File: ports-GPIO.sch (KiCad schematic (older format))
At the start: 3 parts

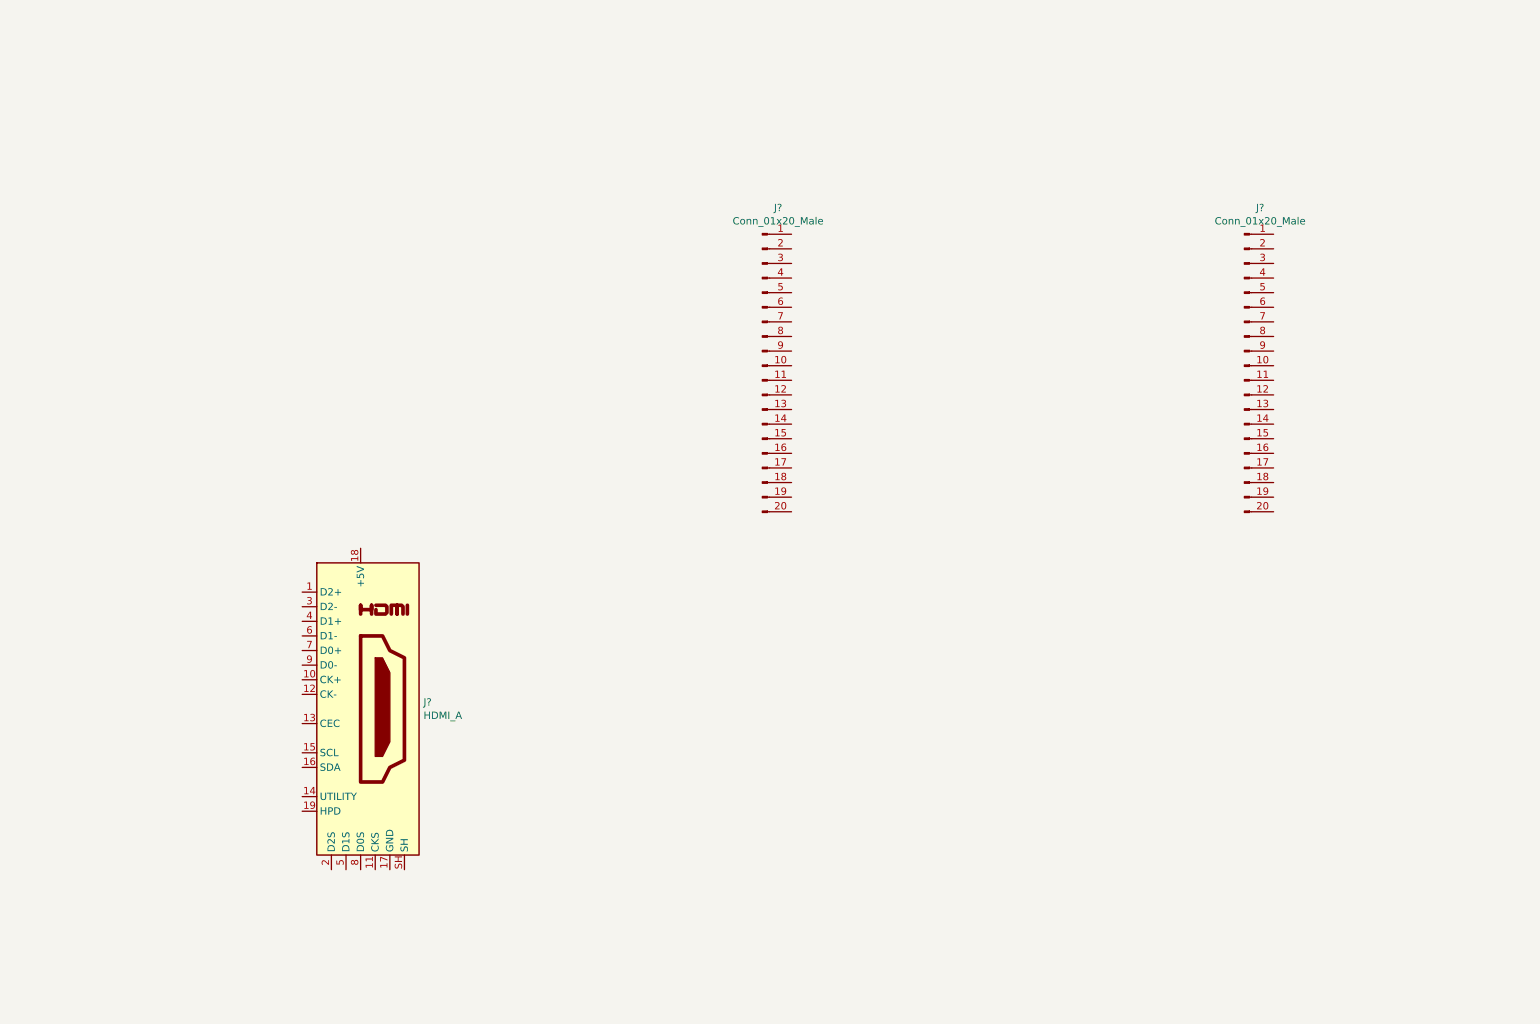
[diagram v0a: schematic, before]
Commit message: broke, out all GPIO and finsihed wiring HDMI
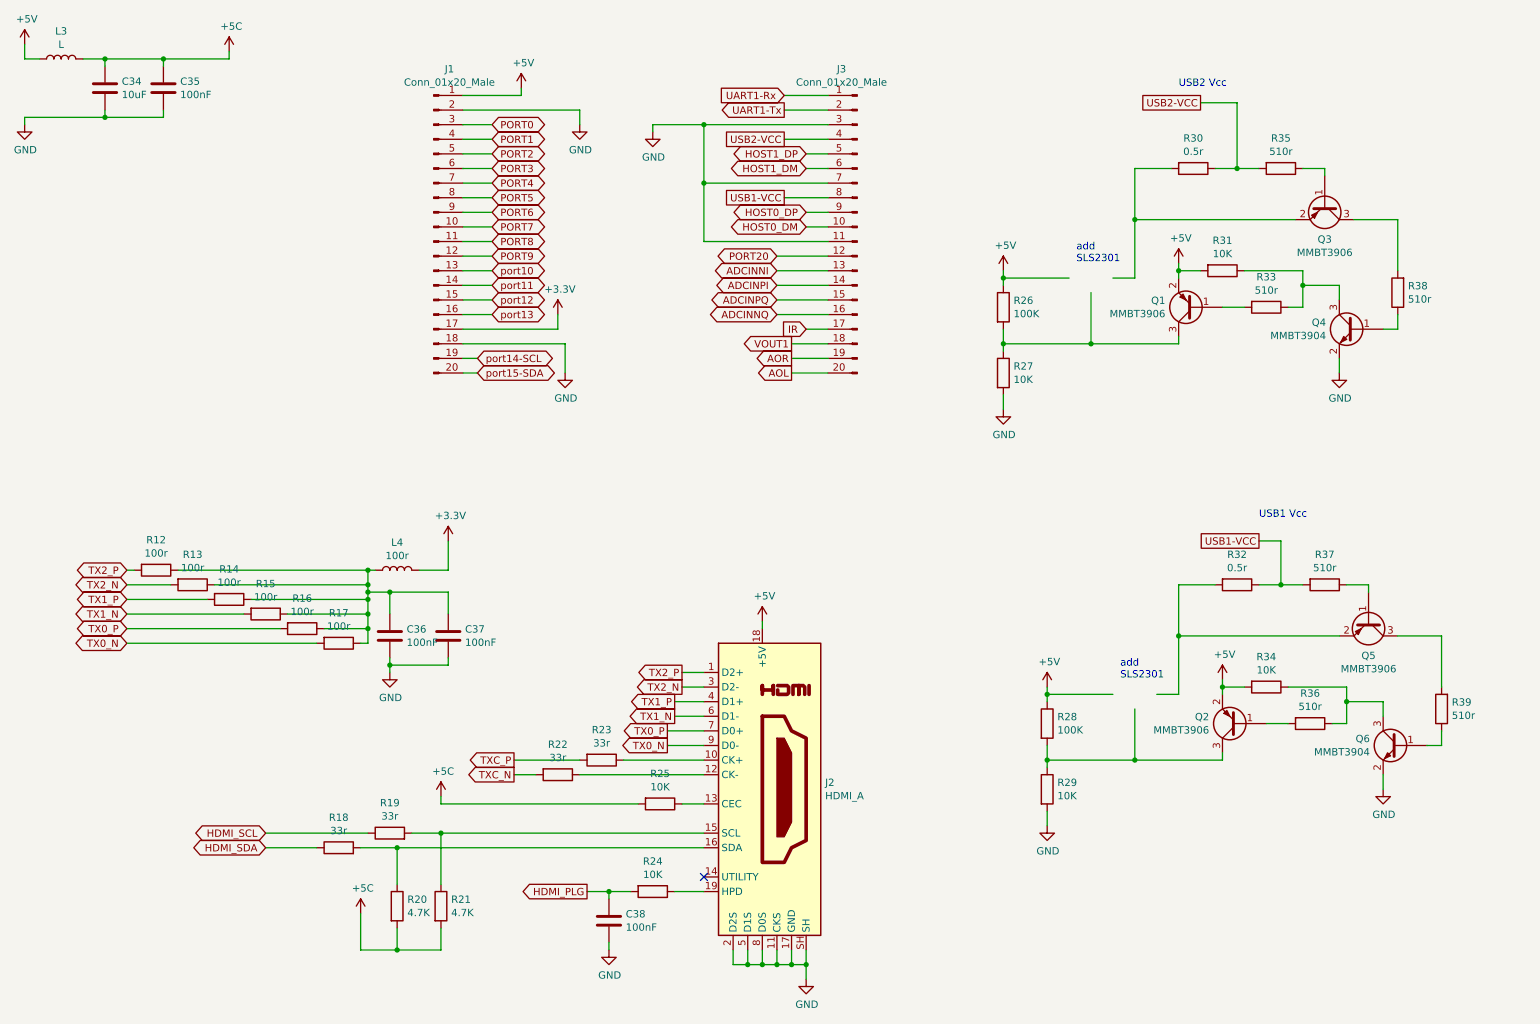
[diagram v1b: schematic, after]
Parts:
- added C34: 10uF, symbol Device:C
- added C35, C36, C37, C38: 100nF, symbol Device:C
- added L3: L, symbol Device:L
- added L4: 100r, symbol Device:L
- added Q1, Q2, Q3, Q5: MMBT3906, Package_TO_SOT_SMD:SOT-23, symbol Transistor_BJT:MMBT3906
- added Q4, Q6: MMBT3904, Package_TO_SOT_SMD:SOT-23, symbol Transistor_BJT:MMBT3904
- added R12, R13, R14, R15, R16, R17: 100r, symbol Device:R
- added R18, R19, R22, R23: 33r, symbol Device:R
- added R20, R21: 4.7K, symbol Device:R
- added R24, R25, R27, R29, R31, R34: 10K, symbol Device:R
- added R26, R28: 100K, symbol Device:R
- added R30, R32: 0.5r, symbol Device:R
- added R33, R35, R36, R37, R38, R39: 510r, symbol Device:R
- gave numbers to parts that had none: 3
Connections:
- net TX2_P: now reaches J2.1 (D2+)
- net TX2_P: now also R12.2
- net at J2.10 (CK+): now also R23.1
- net GND: now reaches J2.11 (CKS)
- net GND: now also J1.18 (Pin_18), J1.2 (Pin_2), J2.17 (GND), J2.2 (D2S), J2.5 (D1S), J2.8 (D0S), J2.SH, J3.11 (Pin_11), J3.3 (Pin_3), J3.7 (Pin_7), C34.2, C35.2, C36.2, C37.2, C38.2, Q4.2 (E), Q6.2 (E), R27.2, R29.2
- net at J2.12 (CK-): now also R22.1
- net at J2.13 (CEC): now also R25.1
- net at J2.15 (SCL): now also R19.2, R21.1
- net at J2.16 (SDA): now also R18.2, R20.1
- net +5V: now reaches J2.18 (+5V)
- net +5V: now also J1.1 (Pin_1), L3.1, Q1.2 (E), Q2.2 (E), R26.1, R28.1, R31.2, R34.2
- net at J2.19 (HPD): now also R24.1
- net TX2_N: now reaches J2.3 (D2-)
- net TX2_N: now also R13.2
- net TX1_P: now reaches J2.4 (D1+)
- net TX1_P: now also R14.2
- net TX1_N: now reaches J2.6 (D1-)
- net TX1_N: now also R15.2
- net TX0_P: now reaches J2.7 (D0+)
- net TX0_P: now also R16.2
- net TX0_N: now reaches J2.9 (D0-)
- net TX0_N: now also R17.2
- net UART1-Rx: now reaches J3.1 (Pin_1)
- net HOST0_DM: now reaches J3.10 (Pin_10)
- net PORT20: now reaches J3.12 (Pin_12)
- net ADCINNI: now reaches J3.13 (Pin_13)
- net ADCINPI: now reaches J3.14 (Pin_14)
- net ADCINPQ: now reaches J3.15 (Pin_15)
- net ADCINNQ: now reaches J3.16 (Pin_16)
- net IR: now reaches J3.17 (Pin_17)
- net VOUT1: now reaches J3.18 (Pin_18)
- net AOR: now reaches J3.19 (Pin_19)
- net UART1-Tx: now reaches J3.2 (Pin_2)
- net AOL: now reaches J3.20 (Pin_20)
- net USB2-VCC: now reaches J3.4 (Pin_4)
- net USB2-VCC: now also R30.1, R35.2
- net HOST1_DP: now reaches J3.5 (Pin_5)
- net HOST1_DM: now reaches J3.6 (Pin_6)
- net USB1-VCC: now reaches J3.8 (Pin_8)
- net USB1-VCC: now also R32.1, R37.2
- net HOST0_DP: now reaches J3.9 (Pin_9)
- net PORT7: now reaches J1.10 (Pin_10)
- net PORT8: now reaches J1.11 (Pin_11)
- net PORT9: now reaches J1.12 (Pin_12)
- net port10: now reaches J1.13 (Pin_13)
- net port11: now reaches J1.14 (Pin_14)
- net port12: now reaches J1.15 (Pin_15)
- net port13: now reaches J1.16 (Pin_16)
- net +3V3: now reaches J1.17 (Pin_17)
- net +3V3: now also L4.2
- net port14-SCL: now reaches J1.19 (Pin_19)
- net port15-SDA: now reaches J1.20 (Pin_20)
- net PORT0: now reaches J1.3 (Pin_3)
- net PORT1: now reaches J1.4 (Pin_4)
- net PORT2: now reaches J1.5 (Pin_5)
- net PORT3: now reaches J1.6 (Pin_6)
- net PORT4: now reaches J1.7 (Pin_7)
- net PORT5: now reaches J1.8 (Pin_8)
- net PORT6: now reaches J1.9 (Pin_9)
- new net: C36.1, C37.1, L4.1, R12.1, R13.1, R14.1, R15.1, R16.1, R17.1
- new net: Q2.3 (C), R28.2, R29.1
- new net: Q2.1 (B), R36.2
- new net: Q6.3 (C), R34.1, R36.1
- new net: Q6.1 (B), R39.1
- new net: Q5.3 (C), R39.2
- new net: Q5.1 (B), R37.1
- new net: Q5.2 (E), R32.2
- new net: Q1.3 (C), R26.2, R27.1
- new net: Q1.1 (B), R33.2
- new net: Q4.3 (C), R31.1, R33.1
- new net: Q4.1 (B), R38.1
- new net: Q3.3 (C), R38.2
- new net: Q3.1 (B), R35.1
- new net: Q3.2 (E), R30.2
- new net +5C: C34.1, C35.1, L3.2, R20.2, R21.2, R25.2
- new net HDMI_PLG: C38.1, R24.2
- new net HDMI_SCL: R19.1
- new net HDMI_SDA: R18.1
- new net TXC_N: R22.2
- new net TXC_P: R23.2
- no-connect marks 0 -> 1
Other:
- note added: "USB1 Vcc"
- note added: "USB2 Vcc"
- note added: "add\nSLS2301"
- moved on the sheet: J1, J2, J3

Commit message: added todo list before i feel aleeped on my keybard*
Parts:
- removed Q2, Q5: MMBT3906, Package_TO_SOT_SMD:SOT-23, symbol Transistor_BJT:MMBT3906
- removed Q6: MMBT3904, Package_TO_SOT_SMD:SOT-23, symbol Transistor_BJT:MMBT3904
- removed R28: 100K, symbol Device:R
- removed R29, R34: 10K, symbol Device:R
- removed R32: 0.5r, symbol Device:R
- removed R36, R37, R39: 510r, symbol Device:R
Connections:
- net labels removed: USB1-VCC
- wire segments 206 -> 173
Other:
- note added: "Reserved for Blue bean WIFI module"
- note removed: "USB1 Vcc"

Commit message: finished scimatic for now, and started populating PCB. *chugs rrum*
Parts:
- added U8: SLS2301, Package_TO_SOT_SMD:SOT-23, symbol Csky:SLS2301
- C34, C35, C36, C37, C38: footprint (none) -> Capacitor_SMD:C_0402_1005Metric
- J1, J3: footprint (none) -> Connector_PinSocket_2.54mm:PinSocket_1x20_P2.54mm_Vertical
- J2: footprint (none) -> Connector_HDMI:HDMI_Micro-D_Molex_46765-0x01
- L3, L4: footprint (none) -> Inductor_SMD:L_0402_1005Metric
- R12, R13, R14, R16, R17: value 100r -> 100R; footprint (none) -> Resistor_SMD:R_0402_1005Metric
- R15: footprint (none) -> Resistor_SMD:R_0402_1005Metric
- R18, R19, R22, R23: value 33r -> 33R; footprint (none) -> Resistor_SMD:R_0402_1005Metric
- R20, R21: value 4.7K -> 4.7k; footprint (none) -> Resistor_SMD:R_0402_1005Metric
- R24, R25, R27, R31: value 10K -> 10k; footprint (none) -> Resistor_SMD:R_0402_1005Metric
- R26: value 100K -> 100k; footprint (none) -> Resistor_SMD:R_0402_1005Metric
- R30: value 0.5r -> 0.5R; footprint (none) -> Resistor_SMD:R_0402_1005Metric
- R33, R35, R38: value 510r -> 510R; footprint (none) -> Resistor_SMD:R_0402_1005Metric
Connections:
- net labels removed: HOST0_DM, HOST0_DP
- wire segments 173 -> 171
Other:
- note removed: "Reserved for Blue bean WIFI module"
- note removed: "add\nSLS2301"
- moved on the sheet: R26, R27

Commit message: started layout of the PCB, allso moved onto craken rum, from captin morgan. please for the love of god check the footprints are right. @MAX
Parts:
- added J4: USB_B_Micro, Connector_USB:USB_Micro-B_Amphenol_10103594-0001LF_Horizontal, symbol Connector:USB_B_Micro
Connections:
- net +5V: now also J4.1 (VBUS)
- net GND: now also J4.5 (GND), J4.6 (Shield)
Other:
- moved on the sheet: Q1, Q3, Q4, R26, R27, R30, R31, R33, R35, R38, U8

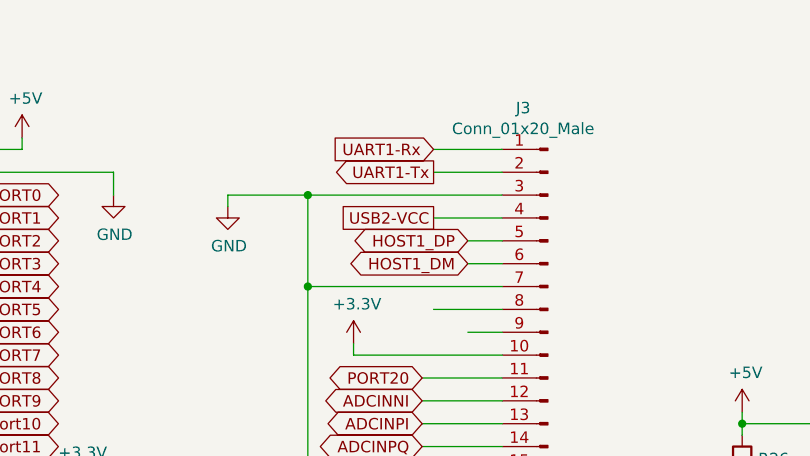
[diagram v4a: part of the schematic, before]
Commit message: started some routing, removed some useless components
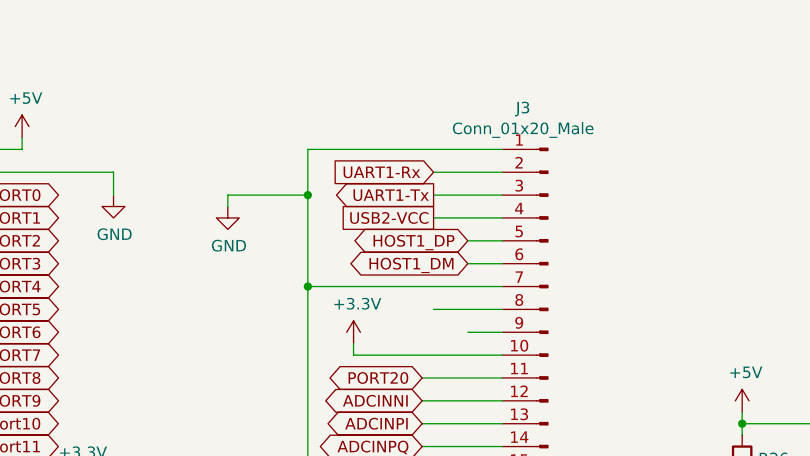
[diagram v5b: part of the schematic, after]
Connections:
- net GND: now also J3.1 (Pin_1); no longer J3.3 (Pin_3)
- net UART1-Rx: now also J3.2 (Pin_2); no longer J3.1 (Pin_1)
- net UART1-Tx: now also J3.3 (Pin_3); no longer J3.2 (Pin_2)
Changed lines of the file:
@@
 Wire Wire Line
 	9250 1650 9400 1650
-Text GLabel 5950 1300 0    50   Output ~ 0
+Text GLabel 5950 1400 0    50   Output ~ 0
 UART1-Tx
-Text GLabel 5950 1200 0    50   Input ~ 0
+Text GLabel 5950 1300 0    50   Input ~ 0
 UART1-Rx
 Text GLabel 3950 1900 2    50   BiDi ~ 0
@@
 	3750 3100 3850 3100
 Wire Wire Line
-	5950 1200 6250 1200
-Wire Wire Line
 	5950 1300 6250 1300
+Wire Wire Line
+	5950 1400 6250 1400
 $Comp
 L power:GND #PWR0157
@@
 Wire Wire Line
 	5400 1800 6250 1800
-Connection ~ 5400 1400
-Wire Wire Line
-	5400 1400 6250 1400
 Wire Wire Line
 	6100 1700 6250 1700
@@
 Wire Wire Line
 	9550 5000 9550 4900
+Wire Wire Line
+	5400 1400 5400 1200
+Wire Wire Line
+	5400 1200 6250 1200
+Connection ~ 5400 1400
 $EndSCHEMATC

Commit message: did more routing
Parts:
- J2: footprint Connector_HDMI:HDMI_Micro-D_Molex_46765-0x01 -> Connector_HDMI:HDMI_A_Contact_Technology_HDMI-19APL2_Horizontal
- J4: footprint Connector_USB:USB_Micro-B_Amphenol_10103594-0001LF_Horizontal -> Connector_USB:USB_Micro-AB_Molex_47590-0001
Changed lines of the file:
@@
 F 0 "J2" H 6230 5996 50  0000 L CNN
 F 1 "HDMI_A" H 6230 5905 50  0000 L CNN
-F 2 "Connector_HDMI:HDMI_Micro-D_Molex_46765-0x01" H 5825 5950 50  0001 C CNN
+F 2 "Connector_HDMI:HDMI_A_Contact_Technology_HDMI-19APL2_Horizontal" H 5825 5950 50  0001 C CNN
 F 3 "https://en.wikipedia.org/wiki/HDMI" H 5825 5950 50  0001 C CNN
 	1    5800 5950
@@
 F 0 "J4" H 9157 5667 50  0000 C CNN
 F 1 "USB_B_Micro" H 9157 5576 50  0000 C CNN
-F 2 "Connector_USB:USB_Micro-B_Amphenol_10103594-0001LF_Horizontal" H 9250 5150 50  0001 C CNN
+F 2 "Connector_USB:USB_Micro-AB_Molex_47590-0001" H 9250 5150 50  0001 C CNN
 F 3 "~" H 9250 5150 50  0001 C CNN
 	1    9100 5200

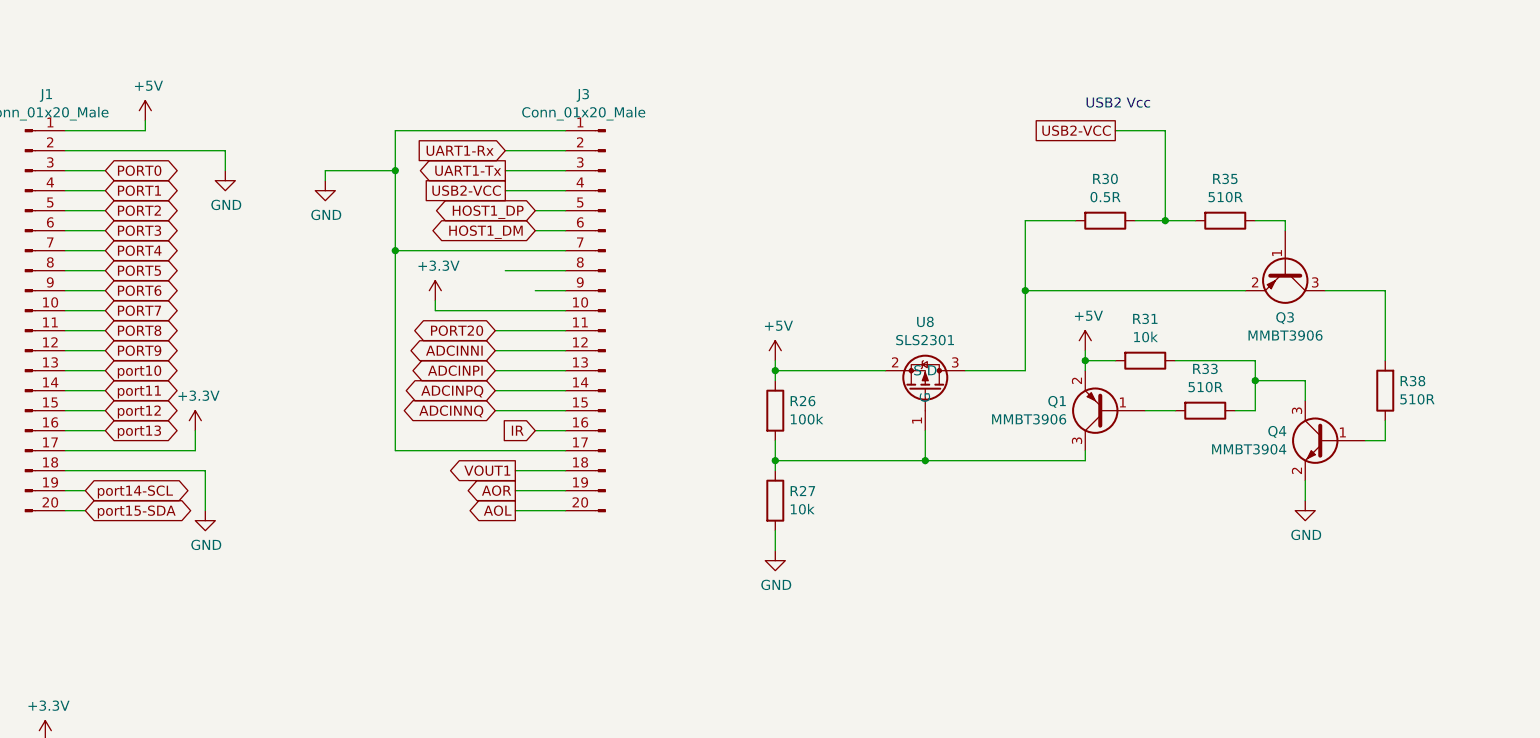
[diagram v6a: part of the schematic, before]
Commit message: removed USB power protection. did more routing
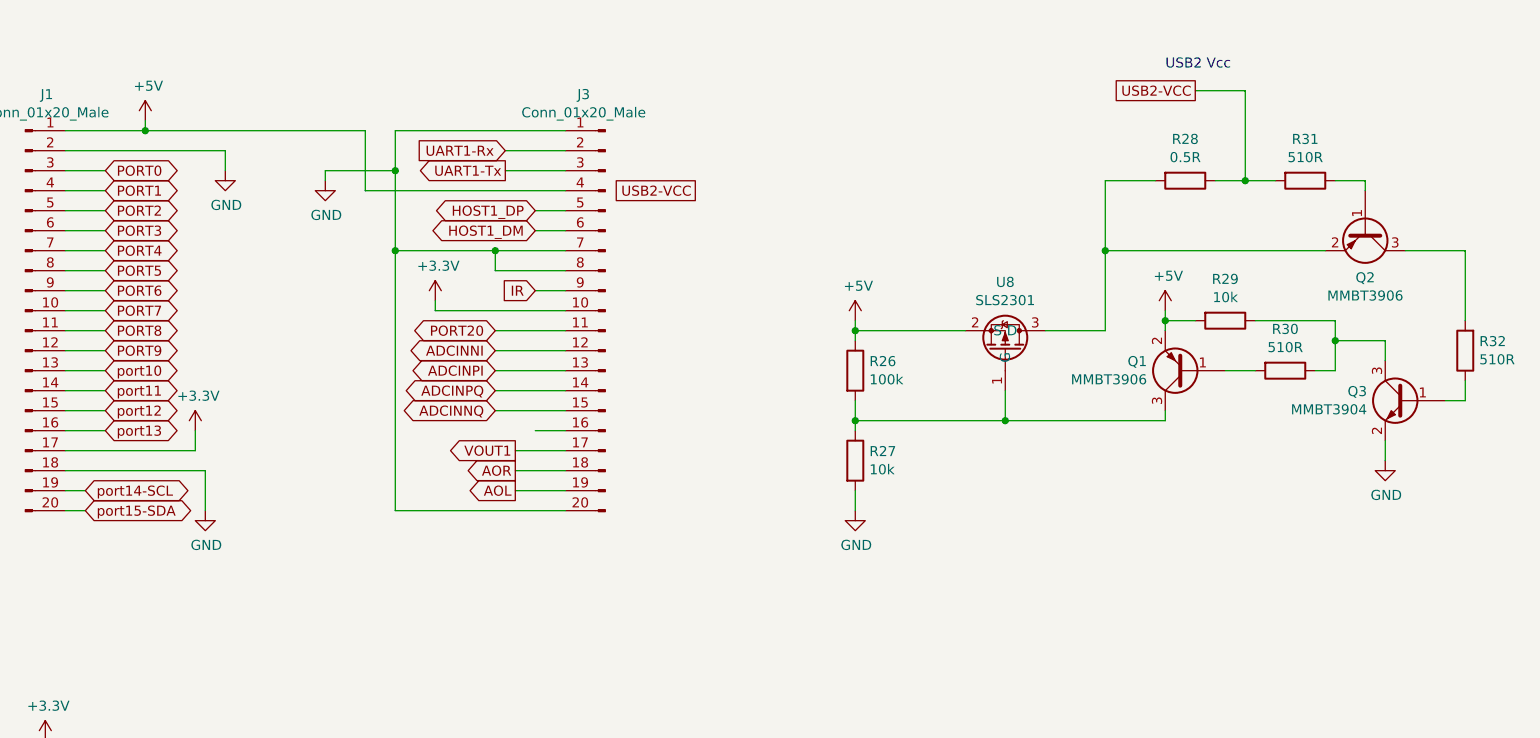
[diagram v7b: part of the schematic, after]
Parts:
- removed Q3: MMBT3906, Package_TO_SOT_SMD:SOT-23, symbol Transistor_BJT:MMBT3906
- removed Q4: MMBT3904, Package_TO_SOT_SMD:SOT-23, symbol Transistor_BJT:MMBT3904
- removed R33, R35, R38: 510R, Resistor_SMD:R_0402_1005Metric, symbol Device:R
- added Q2: MMBT3906, symbol Transistor_BJT:MMBT3906
- added Q3: MMBT3904, symbol Transistor_BJT:MMBT3904
- added R28: 0.5R, symbol Device:R
- added R29: 10k, symbol Device:R
- added R32: 510R, Resistor_SMD:R_0402_1005Metric, symbol Device:R
- Q1, U8: footprint Package_TO_SOT_SMD:SOT-23 -> (none)
- R26, R27: footprint Resistor_SMD:R_0402_1005Metric -> (none)
- R30: value 0.5R -> 510R; footprint Resistor_SMD:R_0402_1005Metric -> (none)
- R31: value 10k -> 510R; footprint Resistor_SMD:R_0402_1005Metric -> (none)
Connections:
- net +5V: now also J3.4 (Pin_4), R29.2; no longer R31.2
- net AOL: now also J3.19 (Pin_19); no longer J3.20 (Pin_20)
- net AOR: now also J3.18 (Pin_18); no longer J3.19 (Pin_19)
- net GND: now also J3.20 (Pin_20), J3.8 (Pin_8), Q3.2 (E); no longer J3.17 (Pin_17)
- net IR: now also J3.9 (Pin_9); no longer J3.16 (Pin_16)
- net USB2-VCC: now also R31.2, R28.1; no longer J3.4 (Pin_4), R30.1
- net VOUT1: now also J3.17 (Pin_17); no longer J3.18 (Pin_18)
- net at R30.2: now also Q1.1 (B); no longer U8.3 (D)
- net at R31.1: now also Q2.1 (B)
- new net: Q3.3 (C), R29.1, R30.1
- new net: Q3.1 (B), R32.1
- new net: Q2.3 (C), R32.2
- new net: Q2.2 (E), R28.2, U8.3 (D)

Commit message: started to add the HDMI port in the pcb
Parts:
- J2: footprint Connector_HDMI:HDMI_A_Contact_Technology_HDMI-19APL2_Horizontal -> C-SKY:HDMI-PCB
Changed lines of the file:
@@
 F 0 "J2" H 6230 5996 50  0000 L CNN
 F 1 "HDMI_A" H 6230 5905 50  0000 L CNN
-F 2 "Connector_HDMI:HDMI_A_Contact_Technology_HDMI-19APL2_Horizontal" H 5825 5950 50  0001 C CNN
+F 2 "C-SKY:HDMI-PCB" H 5825 5950 50  0001 C CNN
 F 3 "https://en.wikipedia.org/wiki/HDMI" H 5825 5950 50  0001 C CNN
 	1    5800 5950
